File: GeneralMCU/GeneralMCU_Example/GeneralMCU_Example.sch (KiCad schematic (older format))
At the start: 1 part, among them U1 SMD42

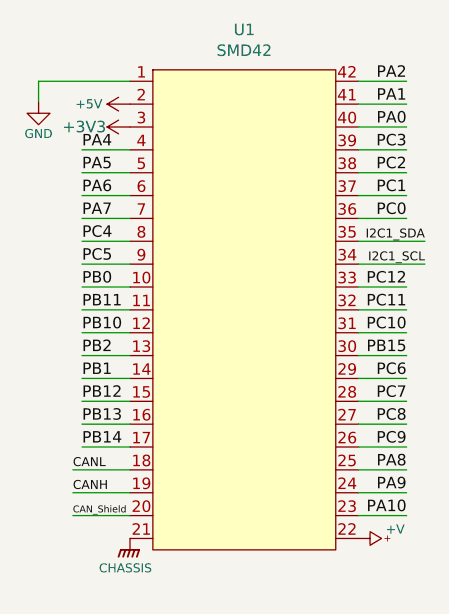
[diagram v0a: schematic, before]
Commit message: Updated Example project and smd sym and footprint for recieving pcbs.
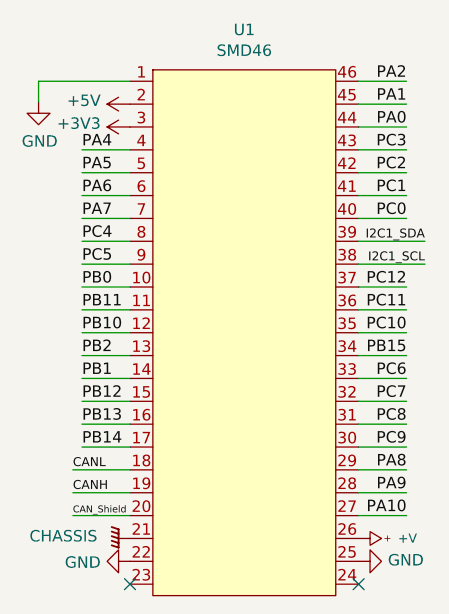
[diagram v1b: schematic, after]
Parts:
- removed U1: SMD42, GeneralMCU_Example:SMD42-FTP, symbol GeneralMCU-Example:SMD42
- added U1: SMD46, GeneralMCU_Example:SMD42-FTP, symbol GeneralMCU-Example:SMD46
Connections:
- net +3V3: now also U1.3
- net +5V: now also U1.2
- net +V: now also U1.26
- net CANH: now also U1.19
- net CANL: now also U1.18
- net CAN_Shield: now also U1.20
- net CHASSIS: now also U1.21
- net GND: now also U1.1, U1.22, U1.25
- net I2C1_SCL: now also U1.38
- net I2C1_SDA: now also U1.39
- net PA0: now also U1.44
- net PA1: now also U1.45
- net PA10: now also U1.27
- net PA2: now also U1.46
- net PA4: now also U1.4
- net PA5: now also U1.5
- net PA6: now also U1.6
- net PA7: now also U1.7
- net PA8: now also U1.29
- net PA9: now also U1.28
- net PB0: now also U1.10
- net PB1: now also U1.14
- net PB10: now also U1.12
- net PB11: now also U1.11
- net PB12: now also U1.15
- net PB13: now also U1.16
- net PB14: now also U1.17
- net PB15: now also U1.34
- net PB2: now also U1.13
- net PC0: now also U1.40
- net PC1: now also U1.41
- net PC10: now also U1.35
- net PC11: now also U1.36
- net PC12: now also U1.37
- net PC2: now also U1.42
- net PC3: now also U1.43
- net PC4: now also U1.8
- net PC5: now also U1.9
- net PC6: now also U1.33
- net PC7: now also U1.32
- net PC8: now also U1.31
- net PC9: now also U1.30
- no-connect marks 0 -> 2
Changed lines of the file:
@@
 EESchema Schematic File Version 4
-LIBS:GeneralMCU-cache
+LIBS:GeneralMCU_Example-cache
 EELAYER 30 0
 EELAYER END
@@
 Comment4 ""
 $EndDescr
-$Comp
-L GeneralMCU-Example:SMD42 U1
-U 1 1 5D9BD874
-P 5730 3110
-F 0 "U1" H 5730 4135 50  0000 C CNN
-F 1 "SMD42" H 5730 4044 50  0000 C CNN
-F 2 "GeneralMCU_Example:SMD42-FTP" H 5730 3110 50  0001 C CNN
-F 3 "" H 5730 3110 50  0001 C CNN
-	1    5730 3110
-	1    0    0    -1
-$EndComp
 Text Label 5020 2610 0    50   ~ 0
 PA4
@@
 Text Label 4980 4210 0    30   ~ 0
 CAN_Shield
-$Comp
-L GeneralMCU-rescue:GND-power #PWR0101
-U 1 1 5DCE40AD
-P 4830 2400
-F 0 "#PWR0101" H 4830 2150 50  0001 C CNN
-F 1 "GND" H 4830 2260 39  0000 C CNN
-F 2 "" H 4830 2400 50  0001 C CNN
-F 3 "" H 4830 2400 50  0001 C CNN
-	1    4830 2400
-	1    0    0    -1
-$EndComp
-$Comp
-L GeneralMCU-rescue:+3V3-power #PWR0102
-U 1 1 5DCE4180
-P 5230 2510
-F 0 "#PWR0102" H 5230 2360 50  0001 C CNN
-F 1 "+3V3" V 5230 2710 50  0000 C CNN
-F 2 "" H 5230 2510 50  0001 C CNN
-F 3 "" H 5230 2510 50  0001 C CNN
-	1    5230 2510
-	0    -1   -1   0
-$EndComp
-$Comp
-L GeneralMCU-rescue:+5V-u104_KICAD_pwr #PWR0103
-U 1 1 5DCE4253
-P 5230 2410
-F 0 "#PWR0103" H 5230 2410 10  0001 C CNN
-F 1 "+5V" V 5230 2590 40  0000 C CNN
-F 2 "" H 5230 2410 60  0000 C CNN
-F 3 "" H 5230 2410 60  0000 C CNN
-	1    5230 2410
-	0    -1   -1   0
-$EndComp
 Wire Wire Line
 	4830 2310 4830 2400
 Wire Wire Line
 	4830 2310 5230 2310
-$Comp
-L GeneralMCU-rescue:+V-u104_KICAD_pwr #PWR0104
-U 1 1 5DCE4326
-P 6230 4310
-F 0 "#PWR0104" H 6230 4310 10  0001 C CNN
-F 1 "+V" V 6190 4470 40  0000 C CNN
-F 2 "" H 6230 4310 60  0000 C CNN
-F 3 "" H 6230 4310 60  0000 C CNN
-	1    6230 4310
-	0    1    1    0
-$EndComp
 Wire Wire Line
 	6520 3110 6230 3110
@@
 PB15
 $Comp
-L GeneralMCU-rescue:CHASSIS-u104_KICAD_pwr #PWR0105
-U 1 1 5DD0A6FE
+L GeneralMCU-Example:SMD46 U1
+U 1 1 5DA3B5F1
+P 5730 3110
+F 0 "U1" H 5730 4135 50  0000 C CNN
+F 1 "SMD46" H 5730 4044 50  0000 C CNN
+F 2 "GeneralMCU_Example:SMD42-FTP" H 5730 3110 50  0001 C CNN
+F 3 "" H 5730 3110 50  0001 C CNN
+	1    5730 3110
+	1    0    0    -1
+$EndComp
+NoConn ~ 6230 4510
+NoConn ~ 5230 4510
+$Comp
+L power:GND #PWR0101
+U 1 1 5DA42B5F
+P 4830 2400
+F 0 "#PWR0101" H 4830 2150 50  0001 C CNN
+F 1 "GND" H 4835 2227 50  0000 C CNN
+F 2 "" H 4830 2400 50  0001 C CNN
+F 3 "" H 4830 2400 50  0001 C CNN
+	1    4830 2400
+	1    0    0    -1
+$EndComp
+$Comp
+L power:+5V #PWR0102
+U 1 1 5DA44F15
+P 5230 2410
+F 0 "#PWR0102" H 5230 2260 50  0001 C CNN
+F 1 "+5V" V 5245 2538 50  0000 L CNN
+F 2 "" H 5230 2410 50  0001 C CNN
+F 3 "" H 5230 2410 50  0001 C CNN
+	1    5230 2410
+	0    -1   -1   0
+$EndComp
+$Comp
+L power:+3V3 #PWR0103
+U 1 1 5DA45501
+P 5230 2510
+F 0 "#PWR0103" H 5230 2360 50  0001 C CNN
+F 1 "+3V3" V 5245 2638 50  0000 L CNN
+F 2 "" H 5230 2510 50  0001 C CNN
+F 3 "" H 5230 2510 50  0001 C CNN
+	1    5230 2510
+	0    -1   -1   0
+$EndComp
+$Comp
+L power:GND #PWR0104
+U 1 1 5DA46D68
+P 5230 4410
+F 0 "#PWR0104" H 5230 4160 50  0001 C CNN
+F 1 "GND" V 5235 4282 50  0000 R CNN
+F 2 "" H 5230 4410 50  0001 C CNN
+F 3 "" H 5230 4410 50  0001 C CNN
+	1    5230 4410
+	0    1    1    0
+$EndComp
+$Comp
+L u104_KICAD_pwr:CHASSIS #PWR0105
+U 1 1 5DA47970
 P 5230 4310
 F 0 "#PWR0105" H 5230 4310 10  0001 C CNN
-F 1 "CHASSIS" H 5210 4180 39  0000 C CNN
+F 1 "CHASSIS" V 5220 3870 50  0000 L CNN
 F 2 "" H 5230 4260 50  0000 C CNN
 F 3 "" H 5230 4260 50  0000 C CNN
 	1    5230 4310
-	1    0    0    -1
+	0    1    1    0
+$EndComp
+$Comp
+L power:GND #PWR0106
+U 1 1 5DA489C3
+P 6230 4410
+F 0 "#PWR0106" H 6230 4160 50  0001 C CNN
+F 1 "GND" V 6235 4282 50  0000 R CNN
+F 2 "" H 6230 4410 50  0001 C CNN
+F 3 "" H 6230 4410 50  0001 C CNN
+	1    6230 4410
+	0    -1   -1   0
+$EndComp
+$Comp
+L u104_KICAD_pwr:+V #PWR0107
+U 1 1 5DA49332
+P 6230 4310
+F 0 "#PWR0107" H 6230 4310 10  0001 C CNN
+F 1 "+V" V 6230 4482 40  0000 L CNN
+F 2 "" H 6230 4310 60  0000 C CNN
+F 3 "" H 6230 4310 60  0000 C CNN
+	1    6230 4310
+	0    1    1    0
 $EndComp
 $EndSCHEMATC
